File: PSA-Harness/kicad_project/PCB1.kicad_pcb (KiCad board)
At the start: 4 copper layers, 22.4 x 46.8 mm, 5 parts, among them J10 B2B_1, J11 B2B_2, J4 to_car_1, J5 to_car_2, J6 to_car_3

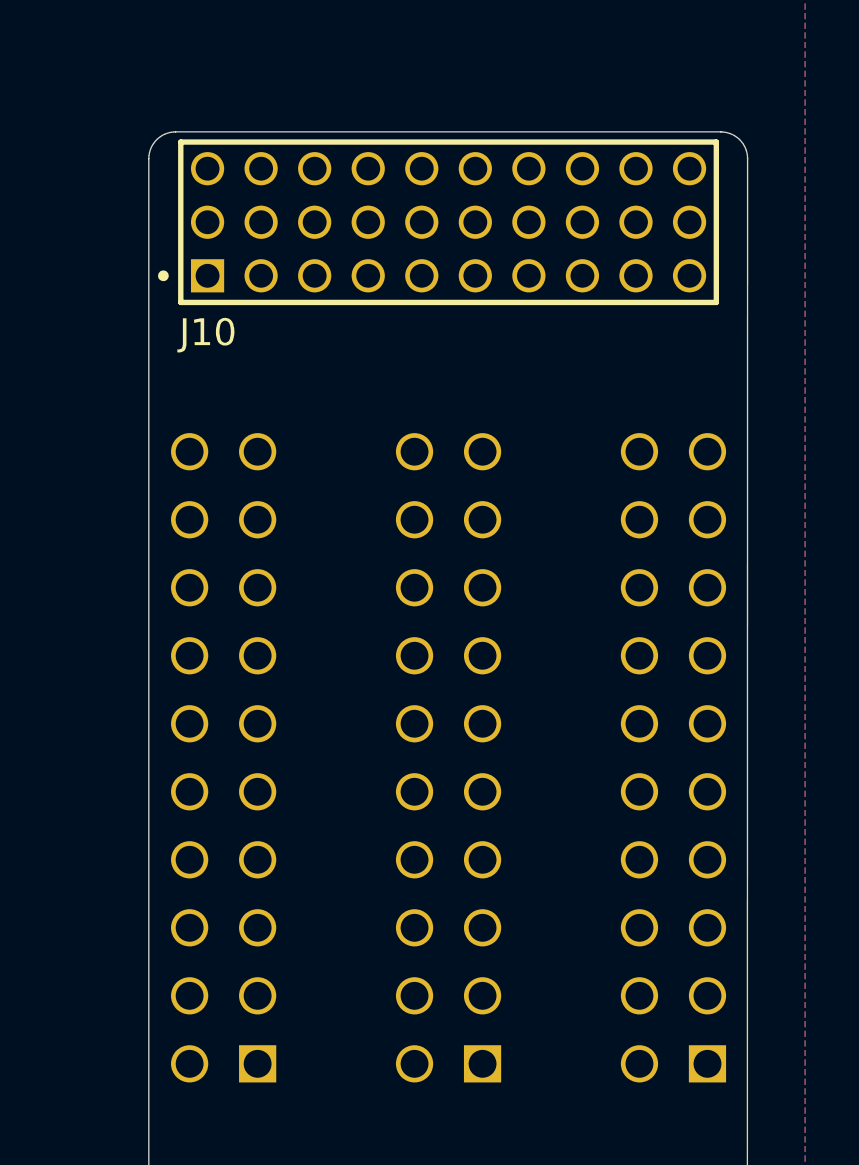
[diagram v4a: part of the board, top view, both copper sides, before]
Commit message: CAN routed
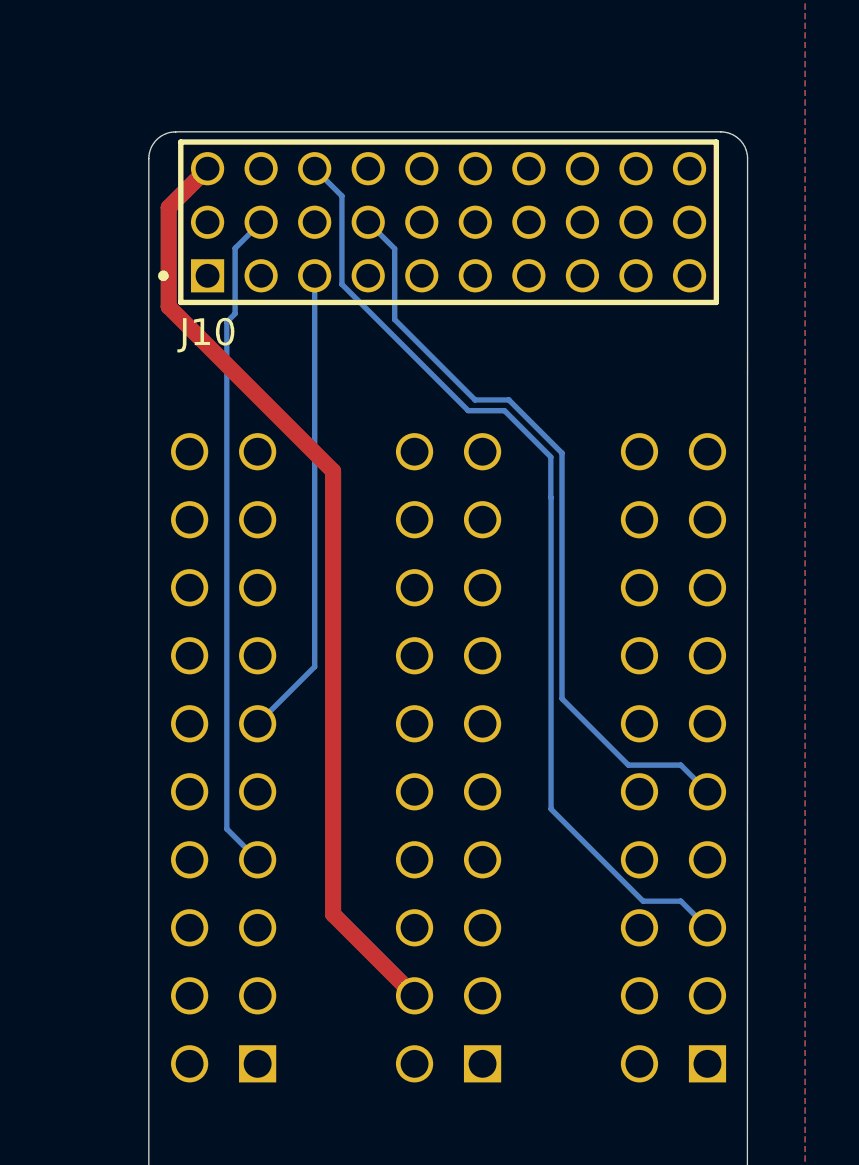
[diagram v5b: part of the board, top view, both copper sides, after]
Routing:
- net CAN2_L: track 0.00 -> 36.0 mm
- net +12V: track 0.00 -> 35.3 mm
- net CAN2_H: track 0.00 -> 28.4 mm
- net CAN1_L: track 0.00 -> 24.8 mm
- net CAN1_H: track 0.00 -> 17.6 mm
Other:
- rule pad_to_mask_clearance: 0.038 -> 0
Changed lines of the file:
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@@
 			(dielectric_constraints no)
 		)
-		(pad_to_mask_clearance 0.038)
+		(pad_to_mask_clearance 0)
 		(allow_soldermask_bridges_in_footprints yes)
 		(tenting front back)
@@
 		)
 	)
+	(segment
+		(start 125.23 105.33)
+		(end 131.37 111.47)
+		(width 0.6)
+		(layer "F.Cu")
+		(net 1)
+	)
+	(segment
+		(start 126.682 100.174)
+		(end 125.23 101.626)
+		(width 0.6)
+		(layer "F.Cu")
+		(net 1)
+	)
+	(segment
+		(start 131.37 111.47)
+		(end 131.37 128.022)
+		(width 0.6)
+		(layer "F.Cu")
+		(net 1)
+	)
+	(segment
+		(start 131.37 128.022)
+		(end 134.412 131.064)
+		(width 0.6)
+		(layer "F.Cu")
+		(net 1)
+	)
+	(segment
+		(start 125.23 101.626)
+		(end 125.23 105.33)
+		(width 0.6)
+		(layer "F.Cu")
+		(net 1)
+	)
+	(segment
+		(start 127.71 103.146)
+		(end 127.71 105.59)
+		(width 0.2)
+		(layer "B.Cu")
+		(net 5)
+	)
+	(segment
+		(start 127.4 105.9)
+		(end 127.4 124.832)
+		(width 0.2)
+		(layer "B.Cu")
+		(net 5)
+	)
+	(segment
+		(start 127.4 124.832)
+		(end 128.552 125.984)
+		(width 0.2)
+		(layer "B.Cu")
+		(net 5)
+	)
+	(segment
+		(start 127.71 105.59)
+		(end 127.4 105.9)
+		(width 0.2)
+		(layer "B.Cu")
+		(net 5)
+	)
+	(segment
+		(start 128.682 102.174)
+		(end 127.71 103.146)
+		(width 0.2)
+		(layer "B.Cu")
+		(net 5)
+	)
+	(segment
+		(start 142.947443 127.528)
+		(end 144.356 127.528)
+		(width 0.2)
+		(layer "B.Cu")
+		(net 6)
+	)
+	(segment
+		(start 139.51 124.090557)
+		(end 142.947443 127.528)
+		(width 0.2)
+		(layer "B.Cu")
+		(net 6)
+	)
+	(segment
+		(start 131.7 101.192)
+		(end 131.7 104.49449)
+		(width 0.2)
+		(layer "B.Cu")
+		(net 6)
+	)
+	(segment
+		(start 136.41551 109.21)
+		(end 137.77 109.21)
+		(width 0.2)
+		(layer "B.Cu")
+		(net 6)
+	)
+	(segment
+		(start 130.682 100.174)
+		(end 131.7 101.192)
+		(width 0.2)
+		(layer "B.Cu")
+		(net 6)
+	)
+	(segment
+		(start 139.51 112.459128)
+		(end 139.51 124.090557)
+		(width 0.2)
+		(layer "B.Cu")
+		(net 6)
+	)
+	(segment
+		(start 139.501436 110.941436)
+		(end 139.501436 112.450565)
+		(width 0.2)
+		(layer "B.Cu")
+		(net 6)
+	)
+	(segment
+		(start 137.77 109.21)
+		(end 139.501436 110.941436)
+		(width 0.2)
+		(layer "B.Cu")
+		(net 6)
+	)
+	(segment
+		(start 139.501436 112.450565)
+		(end 139.51 112.459128)
+		(width 0.2)
+		(layer "B.Cu")
+		(net 6)
+	)
+	(segment
+		(start 131.7 104.49449)
+		(end 136.41551 109.21)
+		(width 0.2)
+		(layer "B.Cu")
+		(net 6)
+	)
+	(segment
+		(start 144.356 127.528)
+		(end 145.352 128.524)
+		(width 0.2)
+		(layer "B.Cu")
+		(net 6)
+	)
+	(segment
+		(start 130.682 118.774)
+		(end 128.552 120.904)
+		(width 0.2)
+		(layer "B.Cu")
+		(net 12)
+	)
+	(segment
+		(start 130.682 104.174)
+		(end 130.682 118.774)
+		(width 0.2)
+		(layer "B.Cu")
+		(net 12)
+	)
+	(segment
+		(start 142.399443 122.448)
+		(end 144.356 122.448)
+		(width 0.2)
+		(layer "B.Cu")
+		(net 13)
+	)
+	(segment
+		(start 137.935686 108.81)
+		(end 139.92 110.794314)
+		(width 0.2)
+		(layer "B.Cu")
+		(net 13)
+	)
+	(segment
+		(start 139.92 110.794314)
+		(end 139.92 119.968557)
+		(width 0.2)
+		(layer "B.Cu")
+		(net 13)
+	)
+	(segment
+		(start 132.682 102.174)
+		(end 133.67 103.162)
+		(width 0.2)
+		(layer "B.Cu")
+		(net 13)
+	)
+	(segment
+		(start 144.356 122.448)
+		(end 145.352 123.444)
+		(width 0.2)
+		(layer "B.Cu")
+		(net 13)
+	)
+	(segment
+		(start 133.67 105.81)
+		(end 136.67 108.81)
+		(width 0.2)
+		(layer "B.Cu")
+		(net 13)
+	)
+	(segment
+		(start 133.67 103.162)
+		(end 133.67 105.81)
+		(width 0.2)
+		(layer "B.Cu")
+		(net 13)
+	)
+	(segment
+		(start 139.92 119.968557)
+		(end 142.399443 122.448)
+		(width 0.2)
+		(layer "B.Cu")
+		(net 13)
+	)
+	(segment
+		(start 136.67 108.81)
+		(end 137.935686 108.81)
+		(width 0.2)
+		(layer "B.Cu")
+		(net 13)
+	)
 	(zone
 		(net 2)
@@
 		(min_thickness 0.25)
 		(filled_areas_thickness no)
-		(fill yes
+		(fill
 			(thermal_gap 0.3)
 			(thermal_bridge_width 0.5)

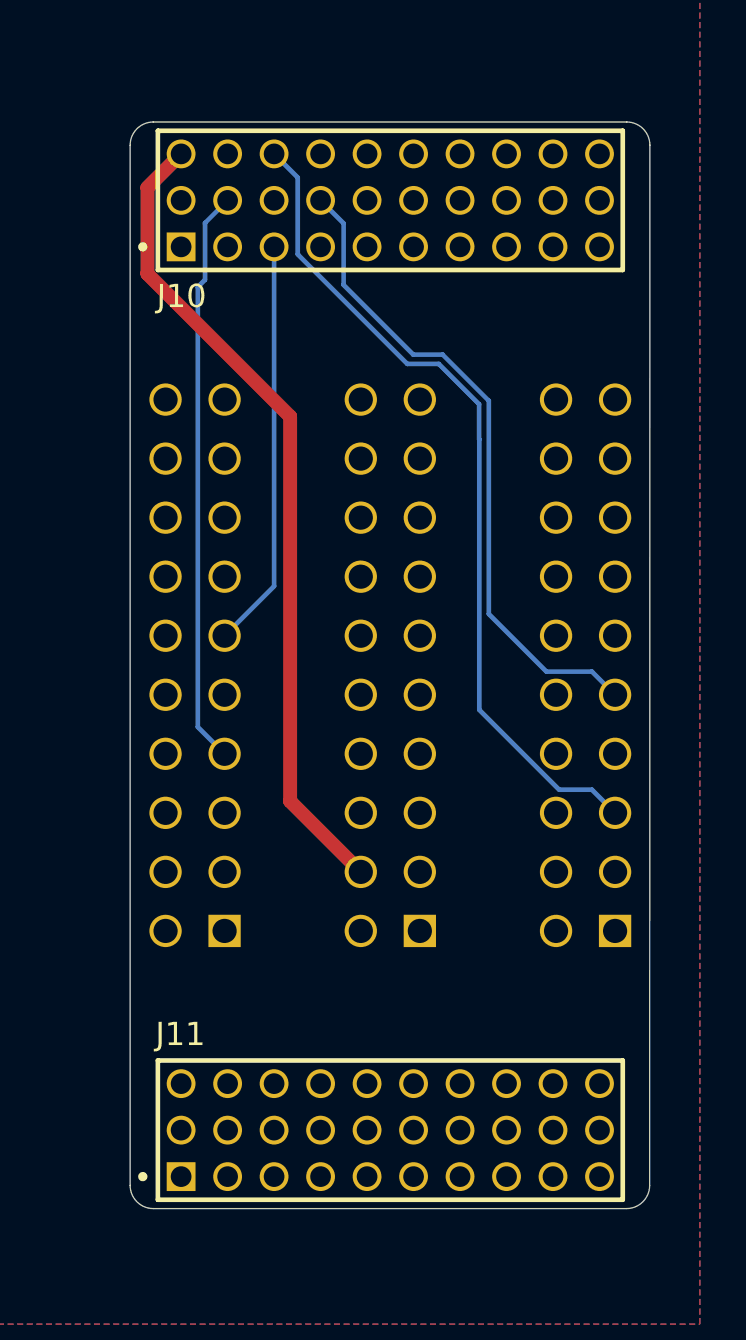
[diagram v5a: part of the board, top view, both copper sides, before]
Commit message: PCB1/2 routed
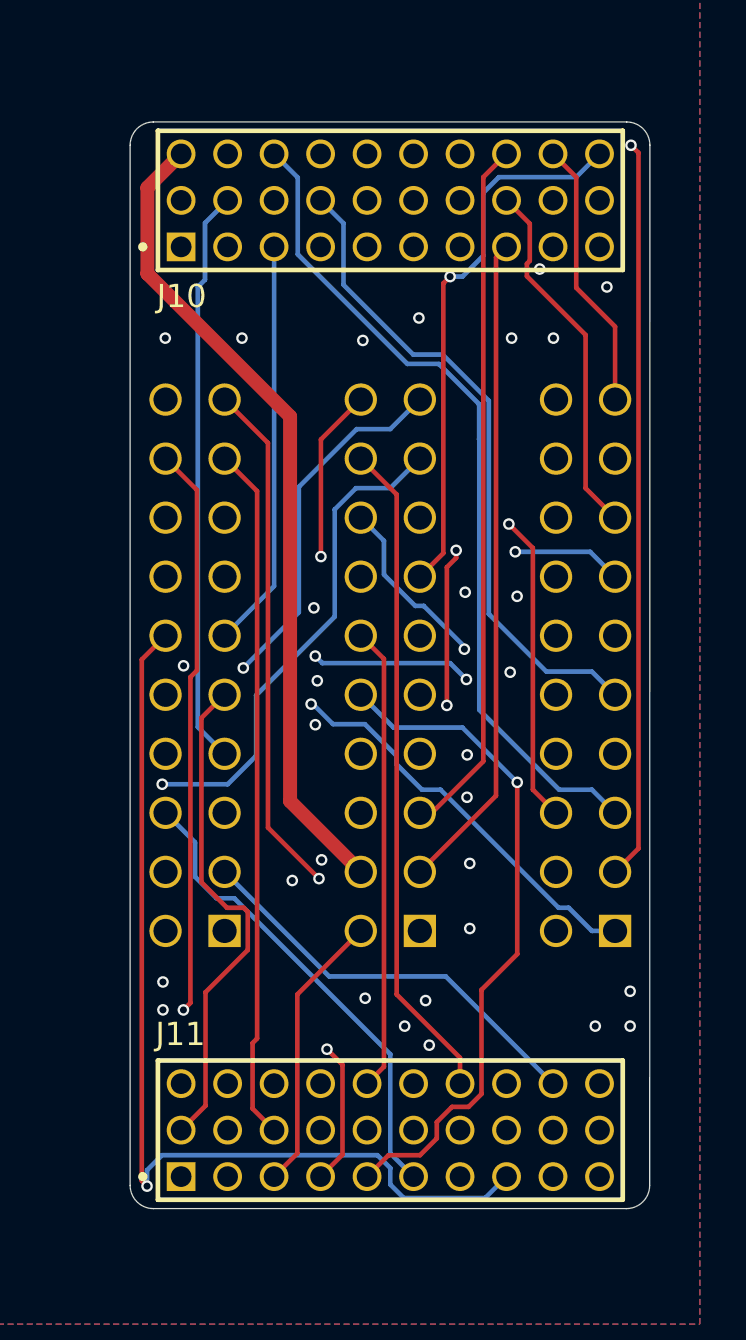
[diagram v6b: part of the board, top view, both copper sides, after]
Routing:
- net 59: track 0.00 -> 47.4 mm, vias 0 -> 1
- net 2: track 0.00 -> 43.8 mm, vias 0 -> 1
- net 28: track 0.00 -> 43.4 mm, vias 0 -> 1
- net 56: track 0.00 -> 42.2 mm, vias 0 -> 1
- net 12: track 0.00 -> 42.2 mm, vias 0 -> 1
- net 60: track 0.00 -> 41.4 mm, vias 0 -> 1
- net 40: track 0.00 -> 40.8 mm, vias 0 -> 4
- net 58: track 0.00 -> 38.2 mm, vias 0 -> 1
- net 1: track 0.00 -> 38.1 mm, vias 0 -> 1
- net 14: track 0.00 -> 37.0 mm, vias 0 -> 1
- net 50: track 0.00 -> 35.9 mm, vias 0 -> 2
- net 30: track 0.00 -> 35.9 mm, vias 0 -> 1
- net 29: track 0.00 -> 35.1 mm, vias 0 -> 1
- net 57: track 0.00 -> 33.9 mm, vias 0 -> 2
- net 11: track 0.00 -> 33.8 mm
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
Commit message: fix DRC errors
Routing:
- net GND: vias 17 -> 18
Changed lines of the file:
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@@
 	)
 	(via
+		(at 130.8 130.5)
+		(size 0.5)
+		(drill 0.3)
+		(layers "F.Cu" "B.Cu")
+		(free yes)
+		(net 2)
+	)
+	(via
 		(at 134.5 108.2)
 		(size 0.5)
@@
 	)
 	(segment
-		(start 135.9553 136.337)
-		(end 135.9553 114.8273)
+		(start 135.9 136.2817)
+		(end 135.9 114.772)
 		(width 0.2)
 		(layer "F.Cu")
@@
 	)
 	(segment
-		(start 135.9553 114.8273)
-		(end 134.412 113.284)
+		(start 138.682 140.174)
+		(end 138.682 139.0637)
 		(width 0.2)
 		(layer "F.Cu")
@@
 	(segment
 		(start 138.682 139.0637)
-		(end 135.9553 136.337)
+		(end 135.9 136.2817)
 		(width 0.2)
 		(layer "F.Cu")
@@
 	)
 	(segment
-		(start 138.682 140.174)
-		(end 138.682 139.0637)
+		(start 135.9 114.772)
+		(end 134.412 113.284)
 		(width 0.2)
 		(layer "F.Cu")
@@
 	(segment
 		(start 128.552 113.284)
-		(end 129.9504 114.6824)
+		(end 130 114.732)
 		(width 0.2)
 		(layer "F.Cu")
@@
 	)
 	(segment
-		(start 129.7575 138.4269)
-		(end 129.7575 141.2495)
+		(start 129.7575 141.2495)
+		(end 130.682 142.174)
 		(width 0.2)
 		(layer "F.Cu")
@@
 	)
 	(segment
-		(start 129.9504 138.234)
+		(start 130 138.1844)
 		(end 129.7575 138.4269)
 		(width 0.2)
@@
 	)
 	(segment
-		(start 129.7575 141.2495)
-		(end 130.682 142.174)
+		(start 129.7575 138.4269)
+		(end 129.7575 141.2495)
 		(width 0.2)
 		(layer "F.Cu")
@@
 	)
 	(segment
-		(start 129.9504 114.6824)
-		(end 129.9504 138.234)
+		(start 130 114.732)
+		(end 130 138.1844)
 		(width 0.2)
 		(layer "F.Cu")
@@
 	)
 	(segment
-		(start 136.682 144.174)
-		(end 135.682 143.174)
+		(start 128.2081 132.2007)
+		(end 127.282 131.2746)
 		(width 0.2)
 		(layer "B.Cu")
@@
 	)
 	(segment
-		(start 135.682 143.174)
-		(end 135.682 138.9092)
+		(start 127.282 131.2746)
+		(end 127.282 129.794)
 		(width 0.2)
 		(layer "B.Cu")
@@
 	)
 	(segment
-		(start 127.282 131.2746)
-		(end 127.282 129.794)
+		(start 135.682 138.782)
+		(end 129.1007 132.2007)
 		(width 0.2)
 		(layer "B.Cu")
@@
 	)
 	(segment
-		(start 135.682 138.9092)
-		(end 128.9735 132.2007)
+		(start 136.682 144.174)
+		(end 135.682 143.174)
 		(width 0.2)
 		(layer "B.Cu")
@@
 	)
 	(segment
-		(start 128.2081 132.2007)
-		(end 127.282 131.2746)
+		(start 129.1007 132.2007)
+		(end 128.2081 132.2007)
 		(width 0.2)
 		(layer "B.Cu")
@@
 	)
 	(segment
-		(start 128.9735 132.2007)
-		(end 128.2081 132.2007)
+		(start 135.682 143.174)
+		(end 135.682 138.782)
 		(width 0.2)
 		(layer "B.Cu")
@@
 	)
 	(segment
-		(start 135.6822 144.5132)
-		(end 135.6822 143.8065)
+		(start 135.0757 143.2)
+		(end 125.9135 143.2)
 		(width 0.2)
 		(layer "B.Cu")
@@
 	)
 	(segment
-		(start 125.2154 143.8981)
-		(end 125.2154 144.5831)
+		(start 140.682 144.174)
+		(end 139.7603 145.0957)
 		(width 0.2)
 		(layer "B.Cu")
@@
 	)
 	(segment
-		(start 125.8612 143.2523)
-		(end 125.2154 143.8981)
+		(start 125.2154 143.8981)
+		(end 125.2154 144.5831)
 		(width 0.2)
 		(layer "B.Cu")
@@
 	)
 	(segment
-		(start 139.7603 145.0957)
-		(end 136.2647 145.0957)
+		(start 135.6822 144.5132)
+		(end 135.6822 143.8065)
 		(width 0.2)
 		(layer "B.Cu")
@@
 	)
 	(segment
-		(start 140.682 144.174)
-		(end 139.7603 145.0957)
+		(start 136.2647 145.0957)
+		(end 135.6822 144.5132)
 		(width 0.2)
 		(layer "B.Cu")
@@
 	)
 	(segment
-		(start 135.128 143.2523)
-		(end 125.8612 143.2523)
+		(start 125.9135 143.2)
+		(end 125.2154 143.8981)
 		(width 0.2)
 		(layer "B.Cu")
@@
 	)
 	(segment
-		(start 136.2647 145.0957)
-		(end 135.6822 144.5132)
+		(start 139.7603 145.0957)
+		(end 136.2647 145.0957)
 		(width 0.2)
 		(layer "B.Cu")
@@
 	(segment
 		(start 135.6822 143.8065)
-		(end 135.128 143.2523)
+		(end 135.0757 143.2)
 		(width 0.2)
 		(layer "B.Cu")
@@
 	)
 	(segment
-		(start 127.5553 124.4407)
-		(end 128.552 123.444)
+		(start 127.5553 131.5082)
+		(end 127.5553 124.4407)
 		(width 0.2)
 		(layer "F.Cu")
@@
 	)
 	(segment
-		(start 127.7319 141.1241)
-		(end 127.7319 136.2407)
+		(start 129.6 132.6)
+		(end 129.2 132.2)
 		(width 0.2)
 		(layer "F.Cu")
@@
 	)
 	(segment
-		(start 127.732 136.2407)
-		(end 129.5487 134.424)
+		(start 129.2 132.2)
+		(end 128.2471 132.2)
 		(width 0.2)
 		(layer "F.Cu")
@@
 	)
 	(segment
-		(start 127.7319 136.2407)
-		(end 127.732 136.2407)
+		(start 127.5553 124.4407)
+		(end 128.552 123.444)
 		(width 0.2)
 		(layer "F.Cu")
@@
 	)
 	(segment
-		(start 129.5487 134.424)
-		(end 129.5487 132.784)
+		(start 128.2471 132.2)
+		(end 127.5553 131.5082)
 		(width 0.2)
 		(layer "F.Cu")
@@
 	)
 	(segment
-		(start 128.6544 132.6073)
-		(end 127.5553 131.5082)
+		(start 127.7319 141.1241)
+		(end 127.7319 136.5681)
 		(width 0.2)
 		(layer "F.Cu")
@@
 	)
 	(segment
-		(start 127.5553 131.5082)
-		(end 127.5553 124.4407)
+		(start 129.6 134.7)
+		(end 129.6 132.6)
 		(width 0.2)
 		(layer "F.Cu")
@@
 	)
 	(segment
-		(start 129.5487 132.784)
-		(end 129.372 132.6073)
+		(start 127.7319 136.5681)
+		(end 129.6 134.7)
 		(width 0.2)
 		(layer "F.Cu")
@@
 		(width 0.2)
 		(layer "F.Cu")
-		(net 53)
-	)
-	(segment
-		(start 129.372 132.6073)
-		(end 128.6544 132.6073)
-		(width 0.2)
-		(layer "F.Cu")

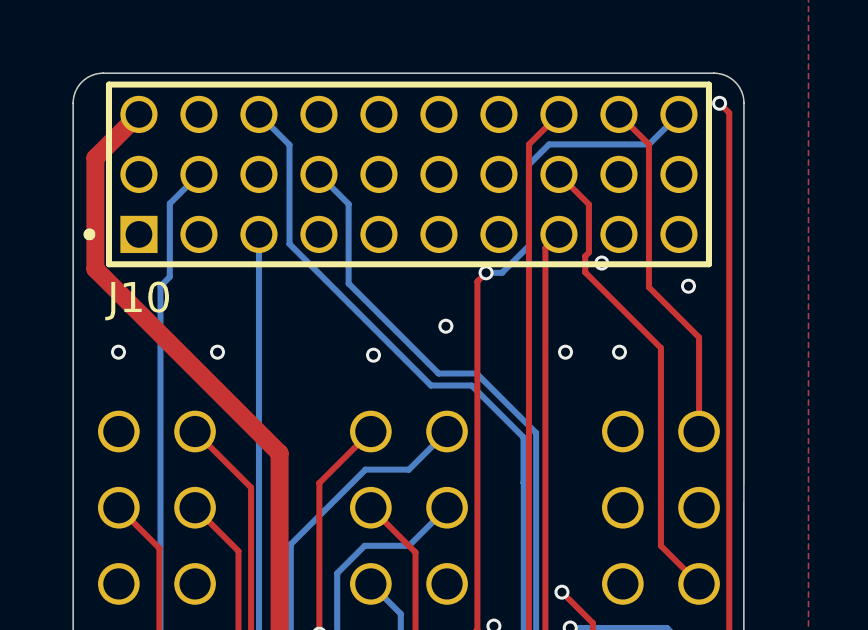
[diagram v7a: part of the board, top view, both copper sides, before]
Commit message: PCB1 add up indicator
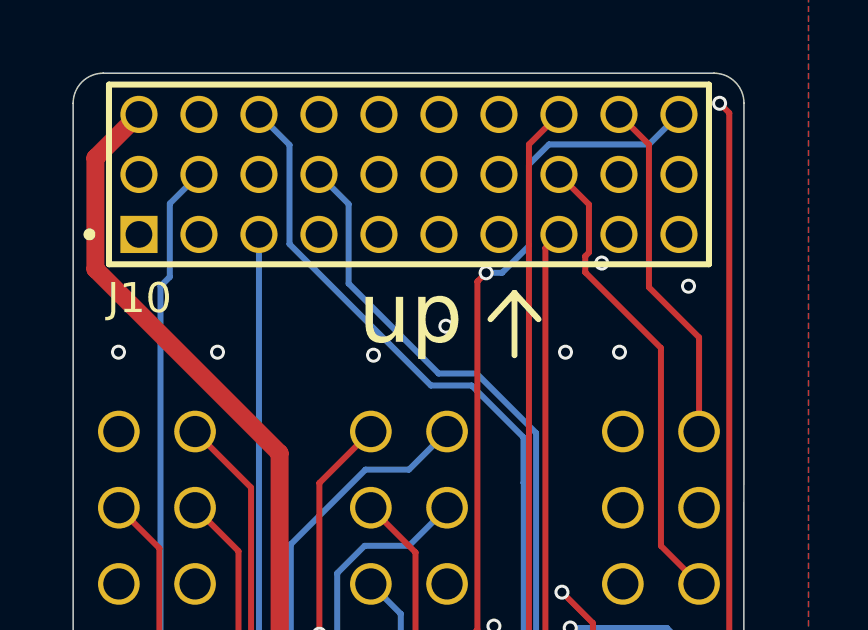
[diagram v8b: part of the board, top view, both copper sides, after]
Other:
- board text added: "up"
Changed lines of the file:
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@@
 		)
+	)
+	(gr_line
+		(start 140 107)
+		(end 139.2 106.125)
+		(stroke
+			(width 0.2)
+			(type solid)
+		)
+		(layer "F.SilkS")
+	)
+	(gr_line
+		(start 139.2 108.2)
+		(end 139.2 106.125)
+		(stroke
+			(width 0.2)
+			(type solid)
+		)
+		(layer "F.SilkS")
+	)
+	(gr_line
+		(start 139.2 106.125)
+		(end 138.4 107)
+		(stroke
+			(width 0.2)
+			(type solid)
+		)
+		(layer "F.SilkS")
 	)
 	(gr_arc
@@
 		(layer "Edge.Cuts")
 	)
+	(gr_text "up"
+		(at 134 108 0)
+		(layer "F.SilkS")
+		(effects
+			(font
+				(size 2 2)
+				(thickness 0.25)
+			)
+			(justify left bottom)
+		)
+	)
 	(gr_text "PCB1"
